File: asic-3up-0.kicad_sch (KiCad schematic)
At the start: 96 parts, among them J3 Conn_01x01, J4 Conn_01x01, U28 MCP1824T-1202E/OT, U29 MCP1824T-1202E/OT, U30 MCP1824T-1202E/OT, U31 SN74AVC4T774, U32 MCP1824T-0802E, U42 MCP1824T-0802E, U43 MCP1824T-0802E, U44 25MHz, U45 BM1362AC_MODE1, U46 BM1362AC_MODE0, U47 BM1362AC_MODE1

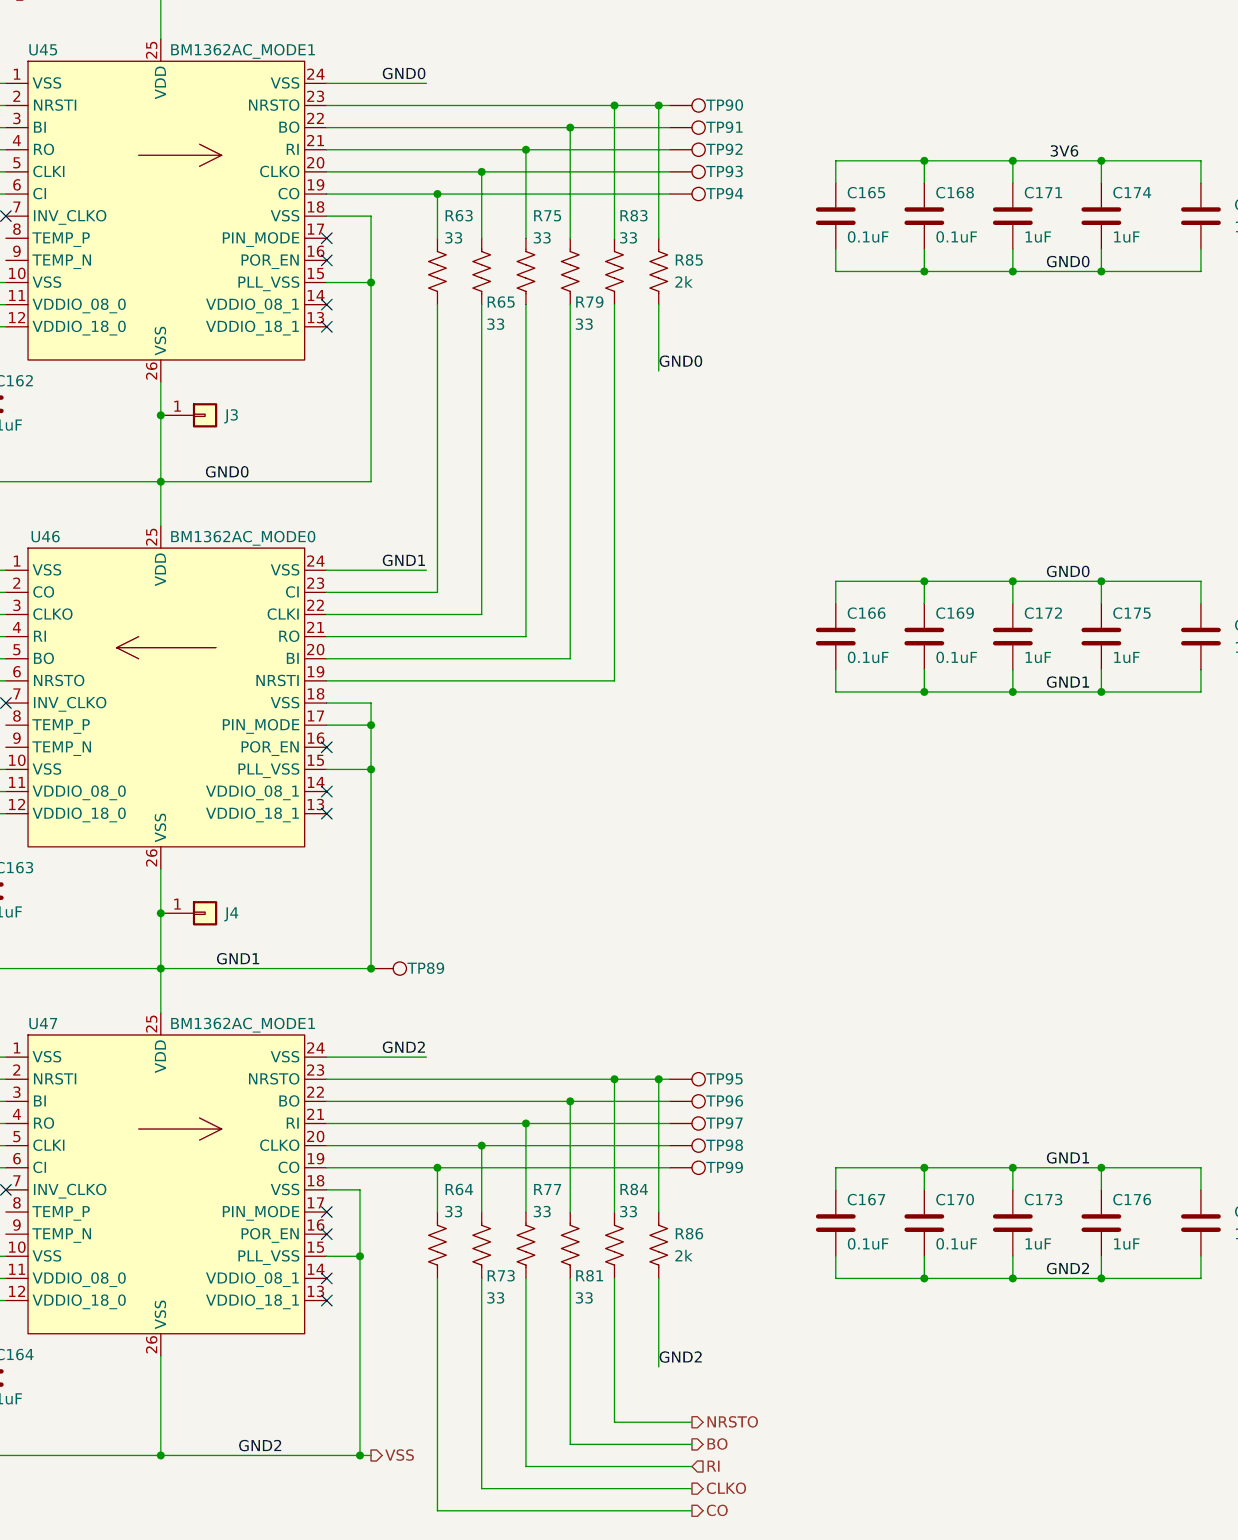
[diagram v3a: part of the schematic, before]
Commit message: so much placing. added mask and paste opening on ASIC footprints. added a pad for a rear heatsink
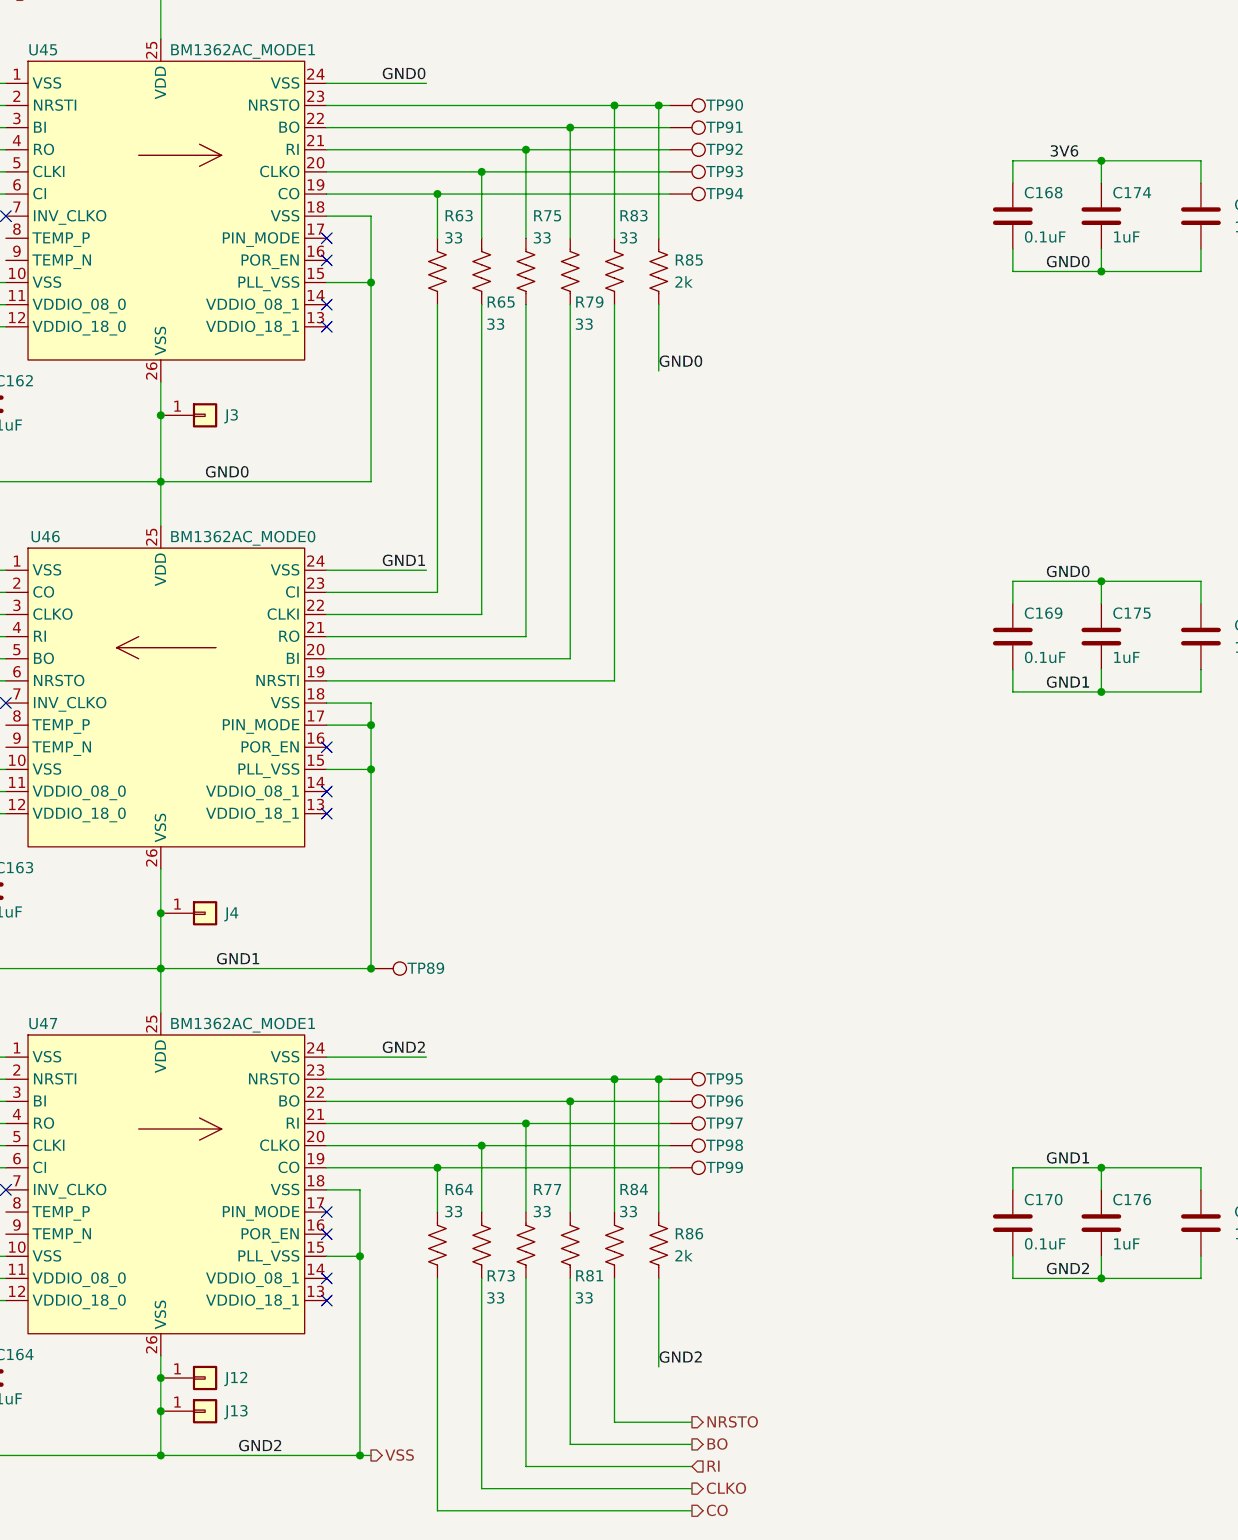
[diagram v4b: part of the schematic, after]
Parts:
- removed C165, C166, C167: 0.1uF, Capacitor_SMD:C_0402_1005Metric, symbol Device:C
- removed C171, C172, C173: 1uF, Capacitor_SMD:C_0402_1005Metric, symbol Device:C
- added J12: Conn_01x01, emberone:14x9_powertab_L, symbol Connector_Generic:Conn_01x01
- added J13: Conn_01x01, emberone:14x9_powertab_R, symbol Connector_Generic:Conn_01x01
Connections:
- net VSS: now also J12.1 (Pin_1), J13.1 (Pin_1)
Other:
- moved on the sheet: C168, C169, C170

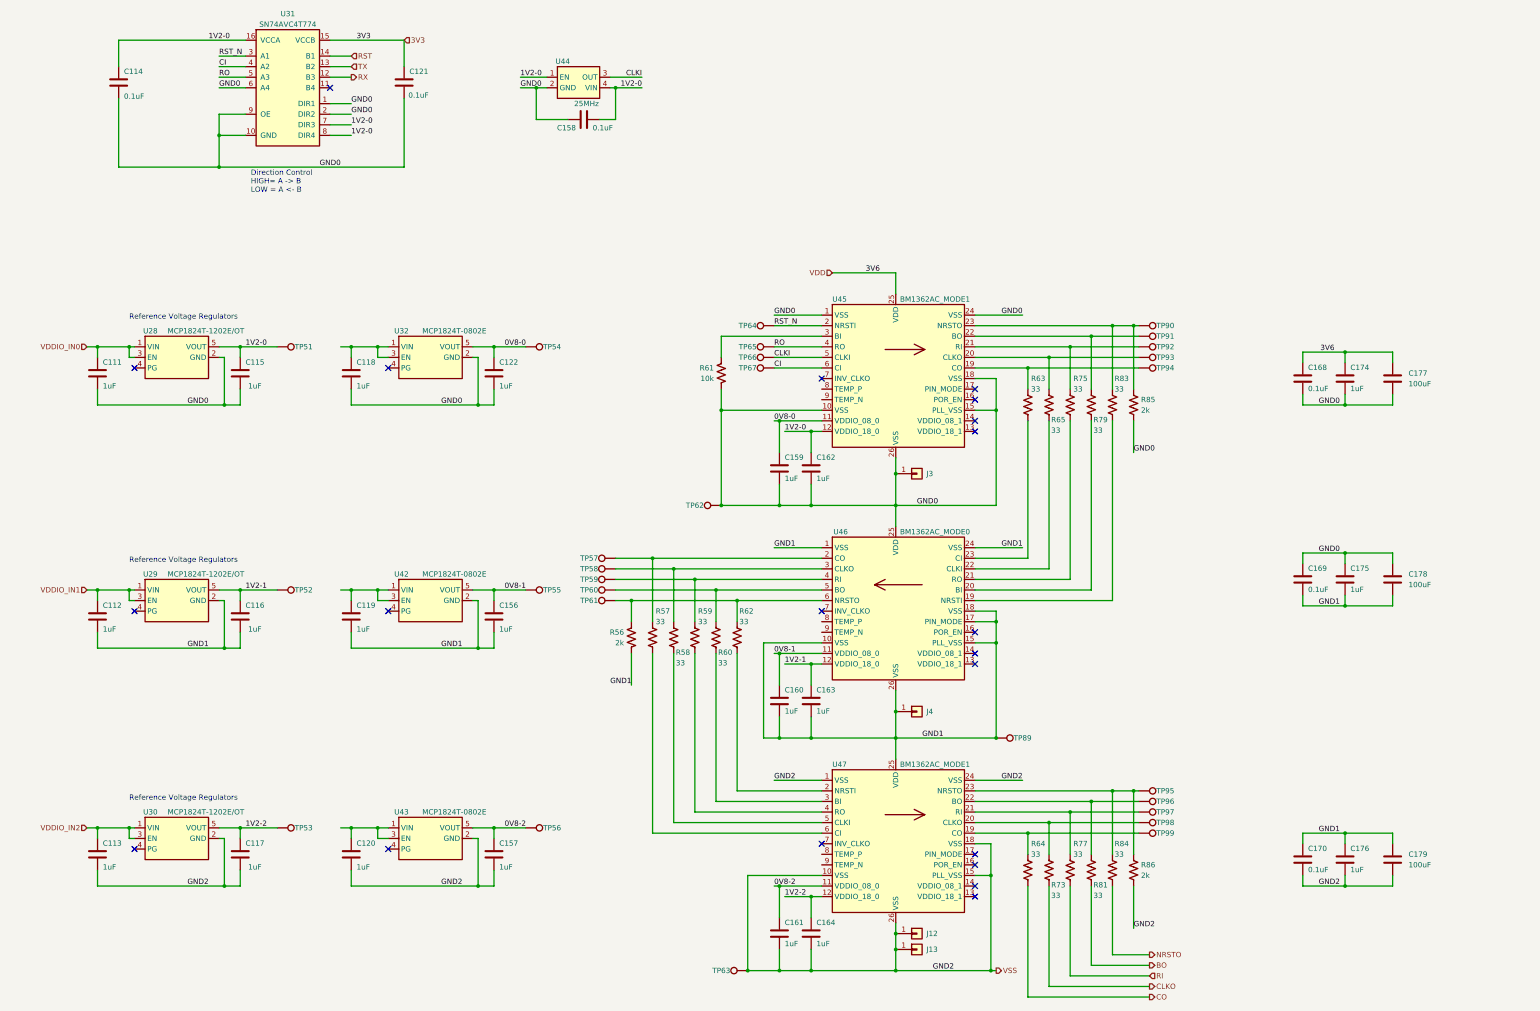
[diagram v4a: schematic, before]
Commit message: forgot that data needs to start with the ASIC that has GND at system GND... reversed everything
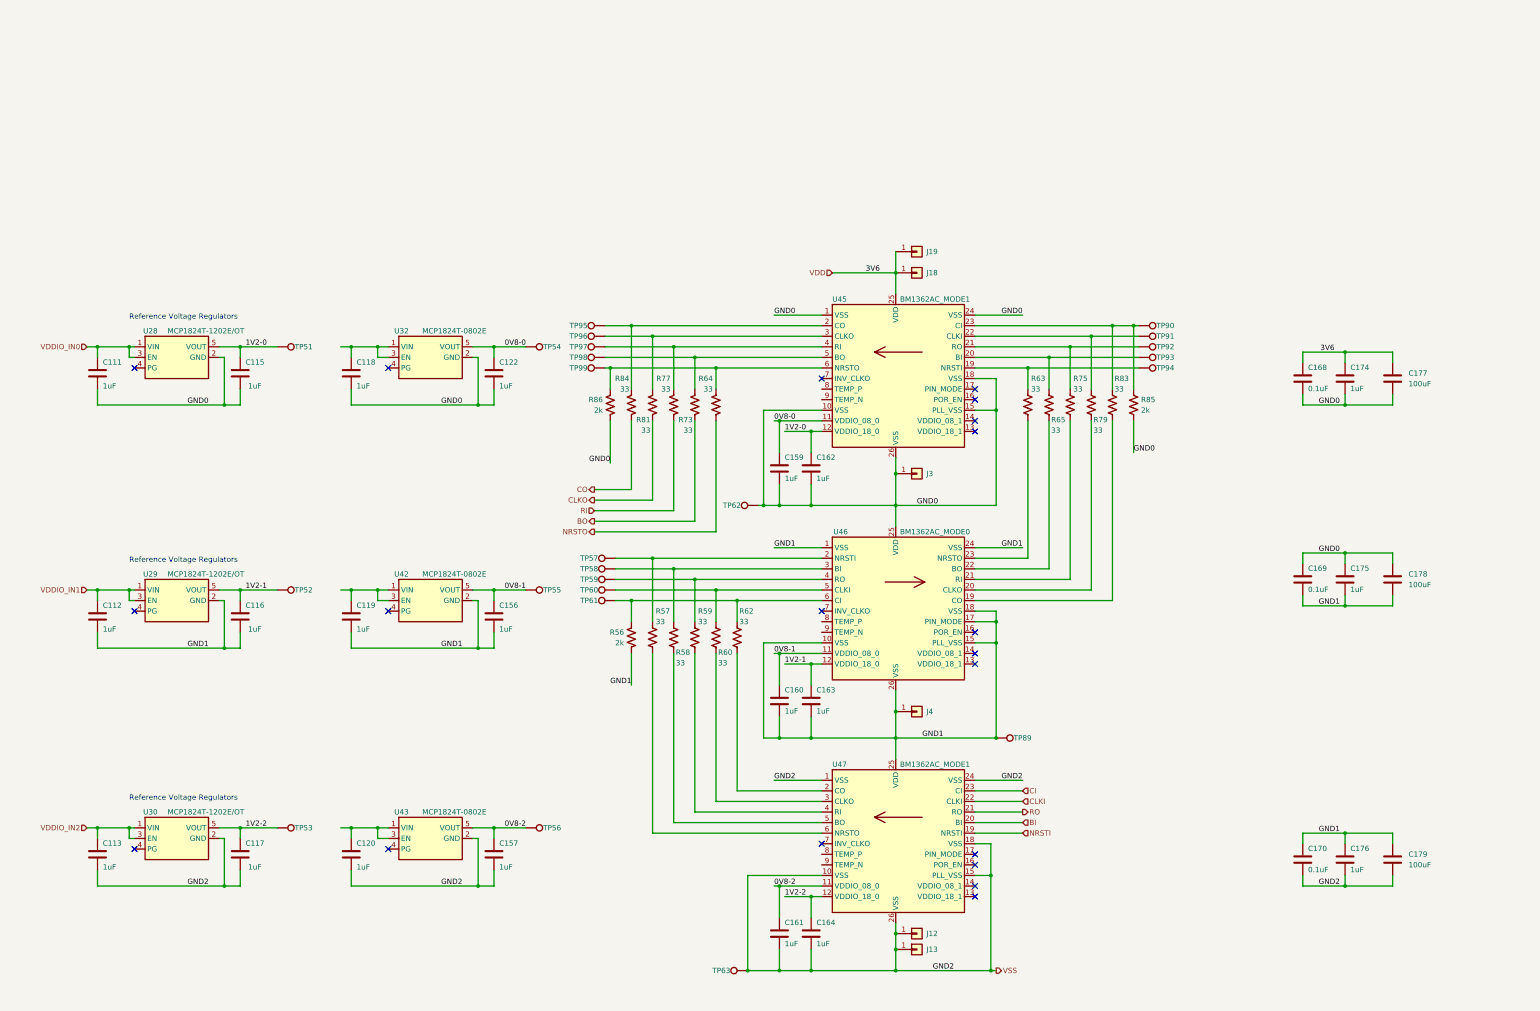
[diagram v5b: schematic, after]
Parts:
- removed C114, C121, C158: 0.1uF, Capacitor_SMD:C_0402_1005Metric, symbol Device:C
- removed R61: 10k, Resistor_SMD:R_0402_1005Metric, symbol Device:R_US
- removed TP64, TP65, TP66, TP67: TestPoint, TestPoint:TestPoint_Pad_D1.5mm, symbol Connector:TestPoint
- removed U31: SN74AVC4T774, Package_SO:TSSOP-16_4.4x5mm_P0.65mm, symbol bitaxe:SN74AVC4T774
- removed U44: 25MHz, bitaxe:SMD3225-4P, symbol bitaxe:oscillator
- added J18, J19: Conn_01x01, emberone:5x9_powertab, symbol Connector_Generic:Conn_01x01
- U45, U47: symbol emberone:BM1362AC_MODE1 -> emberone:BM1362AC_MODE0
- U46: symbol emberone:BM1362AC_MODE0 -> emberone:BM1362AC_MODE1
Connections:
- net RST_N is gone; now on an unnamed net: U45.2 (CO)
- net BO: now also R73.2; no longer R81.2
- net CI: now also U47.23 (CI); no longer U45.6 (CI)
- net CLKI: now also U47.22 (CLKI); no longer U45.5 (CLKI)
- net CLKO: now also R81.2; no longer R73.2
- net CO: now also R84.2; no longer R64.2
- net GND0: now also R86.2
- net NRSTO: now also R64.2; no longer R84.2
- net RO: now also U47.21 (RO); no longer U45.4 (RO)
- net VDD: now also J18.1 (Pin_1), J19.1 (Pin_1)
- net VSS: no longer R86.2
- net at R84.1, TP95.1: no longer R86.1, U47.23 (NRSTO)
- net at R73.1, TP98.1: now also U45.5 (BO); no longer U47.20 (CLKO)
- net at U45.3 (CLKO): now also R81.1, TP96.1
- net at R64.1, TP99.1: now also R86.1, U45.6 (NRSTO); no longer U47.19 (CO)
- net at R77.1, TP97.1: now also U45.4 (RI); no longer U47.21 (RI)
- new net BI: U47.20 (BI)
- new net NRSTI: U47.19 (NRSTI)
- no-connect marks 21 -> 20
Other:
- note removed: "Direction Control HIGH= A -> B LOW = A <- B"
- moved on the sheet: R64, R73, R77, R81, R84, R86, TP62, TP95, TP96, TP97, TP98, TP99

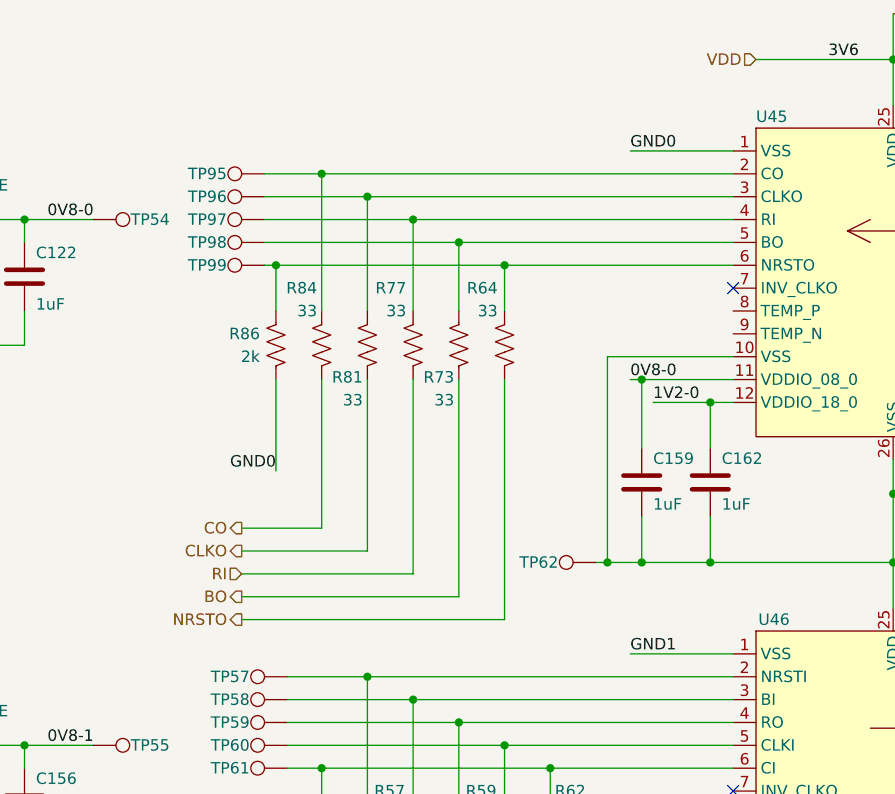
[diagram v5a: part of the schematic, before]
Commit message: placements done. shrunk test points
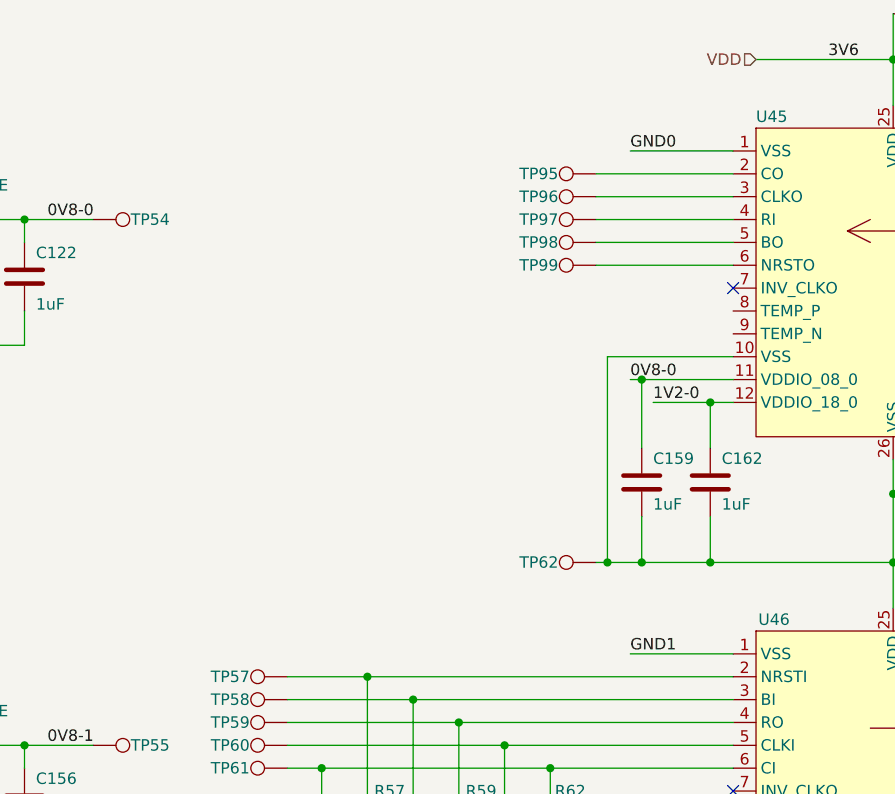
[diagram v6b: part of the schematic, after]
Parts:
- removed R64, R73, R77, R81, R84: 33, Resistor_SMD:R_0402_1005Metric, symbol Device:R_US
- removed R86: 2k, Resistor_SMD:R_0402_1005Metric, symbol Device:R_US
- TP51, TP52, TP53, TP54, TP55, TP56, TP57, TP58, TP59, TP60, TP61, TP62, TP63, TP89, TP90, TP91, TP92, TP93, TP94, TP95, TP96, TP97, TP98, TP99: footprint TestPoint:TestPoint_Pad_D1.5mm -> TestPoint:TestPoint_Pad_D1.0mm
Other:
- moved on the sheet: TP95, TP96, TP97, TP98, TP99
